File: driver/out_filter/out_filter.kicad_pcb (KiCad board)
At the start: 2 copper layers, 64 parts, among them J101 X driver, J102 Y driver, J103 Z driver, J104 Source, J105 I sense, J106 V sense, T201 300:1, T301 300:1, T401 300:1

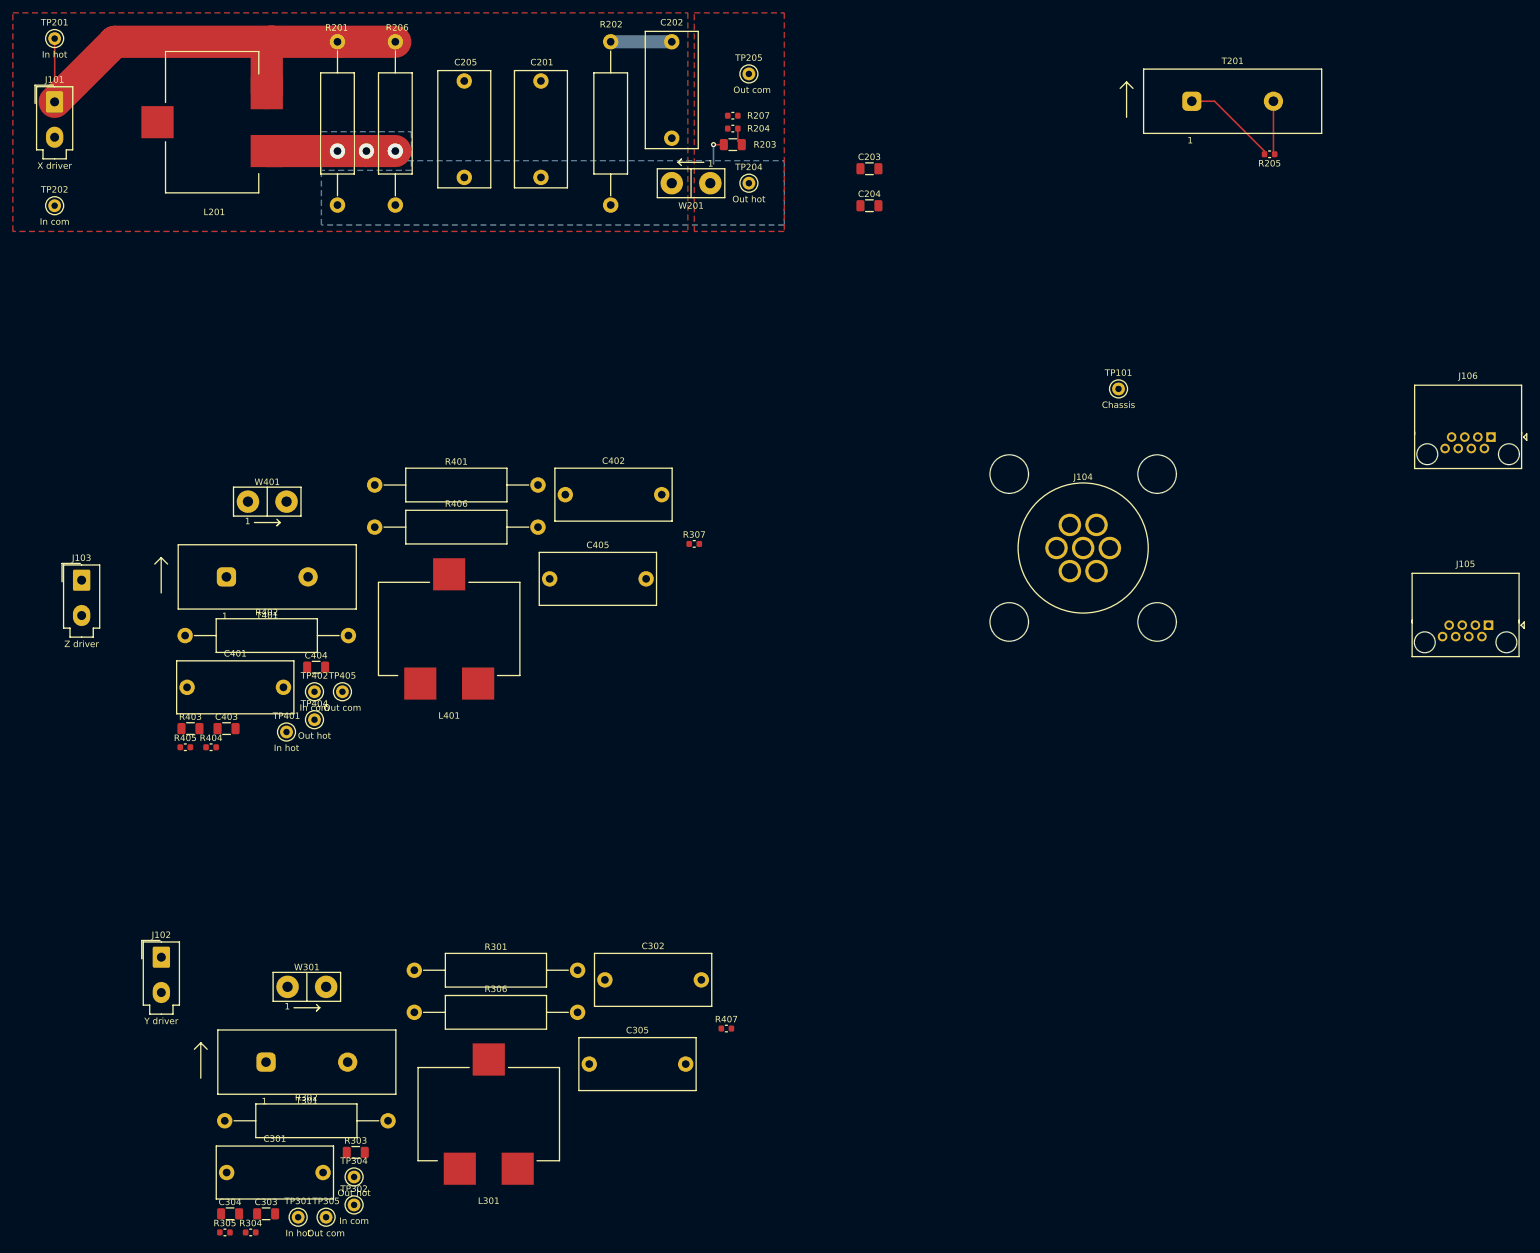
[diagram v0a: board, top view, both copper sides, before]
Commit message: Revision 0 of out_filter board.  Tweaks to footprints, reducing pad size.  General routing and pours.
filter_chan.sch:
deleted some testpoints, added input connector.

out_filter.sch:
Added output connector, changed ground testpoint footprint.
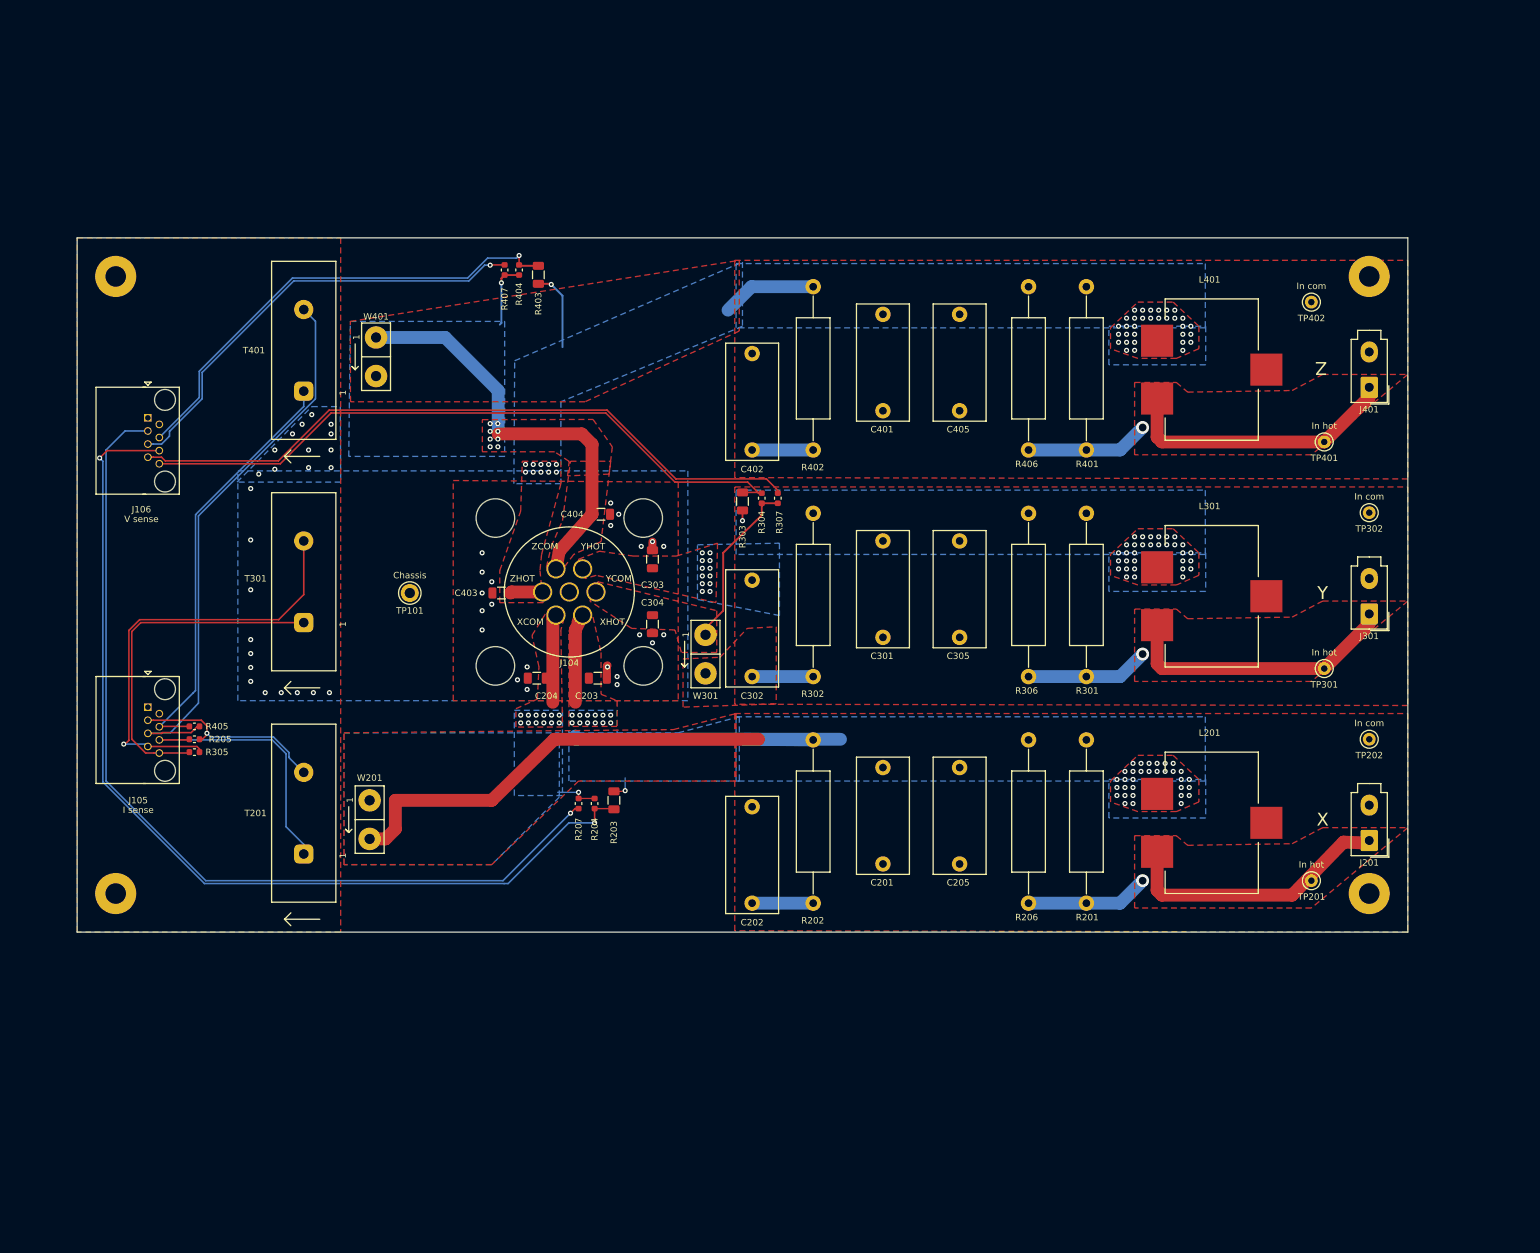
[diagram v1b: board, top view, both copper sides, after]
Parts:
- removed J101: X driver, Connector_Molex:Molex_Mini-Fit_Jr_5566-02A_2x01_P4.20mm_Vertical
- removed J102: Y driver, Connector_Molex:Molex_Mini-Fit_Jr_5566-02A_2x01_P4.20mm_Vertical
- removed J103: Z driver, Connector_Molex:Molex_Mini-Fit_Jr_5566-02A_2x01_P4.20mm_Vertical
- removed TP204, TP304, TP404: Out hot, TestPoint:TestPoint_Keystone_5000-5004_Miniature
- removed TP205, TP305, TP405: Out com, TestPoint:TestPoint_Keystone_5000-5004_Miniature
- added J201: Driver in, Connector_Molex:Molex_Mini-Fit_Jr_5566-02A_2x01_P4.20mm_Vertical, F.Cu at (231.0, 143.8)
- added J301: Driver in, Connector_Molex:Molex_Mini-Fit_Jr_5566-02A_2x01_P4.20mm_Vertical, F.Cu at (231.0, 108.5)
- added J401: Driver in, Connector_Molex:Molex_Mini-Fit_Jr_5566-02A_2x01_P4.20mm_Vertical, F.Cu at (231.0, 73.2)
- added REF**: MountingHole_3.2mm_M3_Pad, MountingHole:MountingHole_3.2mm_M3_Pad, F.Cu at (231.0, 56.0)
- added REF**: MountingHole_3.2mm_M3_Pad, MountingHole:MountingHole_3.2mm_M3_Pad, F.Cu at (231.0, 152.0)
- added REF**: MountingHole_3.2mm_M3_Pad, MountingHole:MountingHole_3.2mm_M3_Pad, F.Cu at (36.0, 152.0)
- added REF**: MountingHole_3.2mm_M3_Pad, MountingHole:MountingHole_3.2mm_M3_Pad, F.Cu at (36.0, 56.0)
- TP101: footprint TestPoint:TestPoint_Keystone_5000-5004_Miniature -> TestPoint:TestPoint_Keystone_5010-5014_Multipurpose
- moved TP201 235.3 mm to (222.0, 150.0), turned to 180 degrees
- moved TP202 220.7 mm to (231.0, 128.0), turned to 180 degrees
- moved J106 209.0 mm to (41.0, 78.0), turned to 90 degrees
- moved J105 208.9 mm to (41.0, 123.0), turned to 90 degrees
- moved TP302 191.1 mm to (231.0, 92.8), turned to 180 degrees
- moved R205 190.4 mm to (48.2, 128.0)
- moved L201 189.9 mm to (206.5, 141.0), turned to 270 degrees
- moved T201 182.1 mm to (65.2, 139.5), turned to 90 degrees
- moved TP301 181.0 mm to (224.0, 117.0), turned to 180 degrees
- moved R201 177.6 mm to (187.0, 153.5), turned to 90 degrees
- moved TP401 167.6 mm to (224.0, 81.8), turned to 180 degrees
- moved TP402 166.5 mm to (222.0, 60.0), turned to 180 degrees
- moved R206 166.3 mm to (178.0, 153.5), turned to 90 degrees
- moved C301 141.7 mm to (155.4, 97.2), turned to 270 degrees
- moved R304 139.2 mm to (136.5, 90.5), turned to 90 degrees
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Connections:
- net Net-(C202-Pad1) renamed /filter_chan_X/SNUB_HOT
- net Net-(C302-Pad1) renamed /filter_chan_Y/SNUB_HOT
- net Net-(C402-Pad1) renamed /filter_chan_Z/SNUB_HOT
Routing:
- net /VX+: track 2.75 -> 152.6 mm, vias 0 -> 2
- net /VX-: track 0.00 -> 143.8 mm, vias 0 -> 1
- net /VY-: track 0.00 -> 107.1 mm
- net /VY+: track 0.00 -> 104.7 mm
- net /IZ-: track 0.00 -> 87.9 mm
- net /ZCOM: track 0.00 -> 76.1 mm, vias 0 -> 9
- net /VZ+: track 0.00 -> 74.6 mm, vias 0 -> 1
- net /VZ-: track 0.00 -> 69.9 mm, vias 0 -> 1
- net /filter_chan_X/IN_COM: track 0.00 -> 69.5 mm
- net /IY-: track 0.00 -> 68.6 mm, vias 0 -> 1
- net /IZ+: track 0.00 -> 67.7 mm
- net /filter_chan_Z/IN_HOT: track 0.00 -> 62.5 mm, vias 0 -> 1
- net /filter_chan_Y/IN_HOT: track 0.00 -> 62.5 mm, vias 0 -> 1
- net /IY+: track 0.00 -> 54.0 mm
- net /XHOT: track 24.6 -> 70.0 mm, vias 4 -> 45
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- added copper zone on B.Cu, net /XCOM
- added copper zone on F.Cu, net /XHOT
- added copper zone on F.Cu, net /YCOM
- added copper zone on B.Cu, net /YHOT
- added copper zone on F.Cu, net /YHOT
- added copper zone on B.Cu, net /ZCOM
- added copper zone on F.Cu, net /ZCOM
- added copper zone on B.Cu, net /ZHOT
- added copper zone on F.Cu, net /ZHOT
- added copper zone on F.Cu, net /filter_chan_X/IN_HOT
- added copper zone on F.Cu, net /filter_chan_Y/IN_COM
- added copper zone on F.Cu, net /filter_chan_Y/IN_HOT
- added copper zone on F.Cu, net /filter_chan_Z/IN_COM
- added copper zone on F.Cu, net /filter_chan_Z/IN_HOT
- added copper zone on B.Cu, net Earth
- added copper zone on F.Cu, net Earth
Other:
- board outline added: 207 x 108 mm
- net class Com added: clearance 0.2, trace_width 2, via_dia 2.4, via_drill 1.2
- net class Hot added: clearance 0.9, trace_width 2, via_dia 2.4, via_drill 1.2
- board text added: "X"
- board text added: "XCOM"
- board text added: "XHOT"
- board text added: "Y"
- board text added: "YCOM"
- board text added: "YHOT"
- board text added: "Z"
- board text added: "ZCOM"
- board text added: "ZHOT"

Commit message: Checkpoint before I start ripping the chassis ground components out of input_board.
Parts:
- C201, C205, C301: value C_out -> 470 nF
- C202, C302: value C_snub -> DNP
- C305, C405: value C_out -> DNP
- C401: value C_out -> 100 nF
- C402: value C_snub -> 100 nF
- R201, R206, R306: value R_shunt -> 15
- R202, R302: value R_snub -> DNP
- R301, R401, R406: value R_shunt -> DNP
- R402: value R_snub -> 47
- moved R205 20.5 mm to (68.8, 128.0)
- moved R305 20.5 mm to (68.8, 130.0)
- moved R405 20.5 mm to (68.8, 126.0)
- moved C201 20.0 mm to (175.4, 132.4)
- moved C202 20.0 mm to (155.0, 153.5)
- moved C203 20.0 mm to (131.0, 118.5)
- moved C204 20.0 mm to (121.5, 118.5)
- moved C205 20.0 mm to (187.3, 132.4)
- moved C301 20.0 mm to (175.4, 97.2)
- moved C302 20.0 mm to (155.0, 118.2)
- moved C303 20.0 mm to (139.5, 100.0)
- moved C304 20.0 mm to (139.5, 110.1)
- moved C305 20.0 mm to (187.3, 97.2)
- moved C401 20.0 mm to (175.4, 61.9)
- moved C402 20.0 mm to (155.0, 83.0)
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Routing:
- net /IX+: track 42.1 -> 40.5 mm
- net /IZ+: track 67.7 -> 66.9 mm
- net /VY+: track 104.7 -> 104.0 mm
- net /VX+: track 152.6 -> 153.3 mm
- net /VZ-: track 69.9 -> 70.4 mm
- net /IY+: track 54.0 -> 54.5 mm
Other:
- board text added: "Component values differ between channels, with some footprints unpopulated. Correct values are set for the "value" in this PCB, but are not directly in the schematic design because the subsheets force the component values the same. 470 nF: C201, C205, C301 15 Ohm: R201, R206, R306 100 nF: C402, C405 47 Ohm: R402 Do not place: C202, R202, R301, C305, R302, C302, R401, R406, C401"
- board text added: "Current transformer primaries are 3 turns on T201, T301, T401. Use 16 ga wire jumpers. W201 goes to T201, etc. Three turns means three passes through the center of the transformer, starting from jumper pad 1, thru center hole in the arrow direction (right to left), around the side of the transformer and back thru 2 more times. The last half-turn passes around the outside of the core, returning to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"
